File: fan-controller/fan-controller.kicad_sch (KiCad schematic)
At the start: 0 parts

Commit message: Add Seeed XIAO ESP32-C3 module to schematic
Vendored Seeed's official OPL KiCad library (symbol + SMD/DIP footprints)
for the XIAO series into fan-controller/libraries/, with project-local
sym-lib-table/fp-lib-table pointing at it. Placed U1 as the XIAO
ESP32-C3, using the DIP footprint (14 through-hole-style pads matching
the module's usable pins) since it'll be socketed via female headers
rather than soldered direct.
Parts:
- added U1: XIAO ESP32-C3, Seeed_Studio_XIAO_Series:XIAO-ESP32-C3-DIP, symbol Seeed_Studio_XIAO_Series:XIAO-ESP32-C3-SMD
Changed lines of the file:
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@@
 		)
 	)
+  (symbol (lib_id "Seeed_Studio_XIAO_Series:XIAO-ESP32-C3-SMD") (at 150.0 100.0 0) (unit 1)
+  (exclude_from_sim no) (in_bom yes) (on_board yes) (dnp no)
+  (property "Reference" "U1" (at 150.0 95.0 0)
+    (effects (font (size 1.27 1.27)))
+  )
+  (property "Value" "XIAO ESP32-C3" (at 150.0 102.54 0)
+    (effects (font (size 1.27 1.27)))
+  )
+  (property "Footprint" "Seeed_Studio_XIAO_Series:XIAO-ESP32-C3-DIP" (at 150.0 105.08 0)
+    (effects (font (size 1.27 1.27)) (hide yes))
+  )
+    (pin "1")
+    (pin "2")
+    (pin "3")
+    (pin "4")
+    (pin "5")
+    (pin "6")
+    (pin "7")
+    (pin "8")
+    (pin "9")
+    (pin "10")
+    (pin "11")
+    (pin "12")
+    (pin "13")
+    (pin "14")
+    (pin "15")
+    (pin "16")
+    (pin "17")
+    (pin "18")
+    (pin "19")
+    (pin "20")
+    (pin "21")
+    (pin "22")
 )
+)

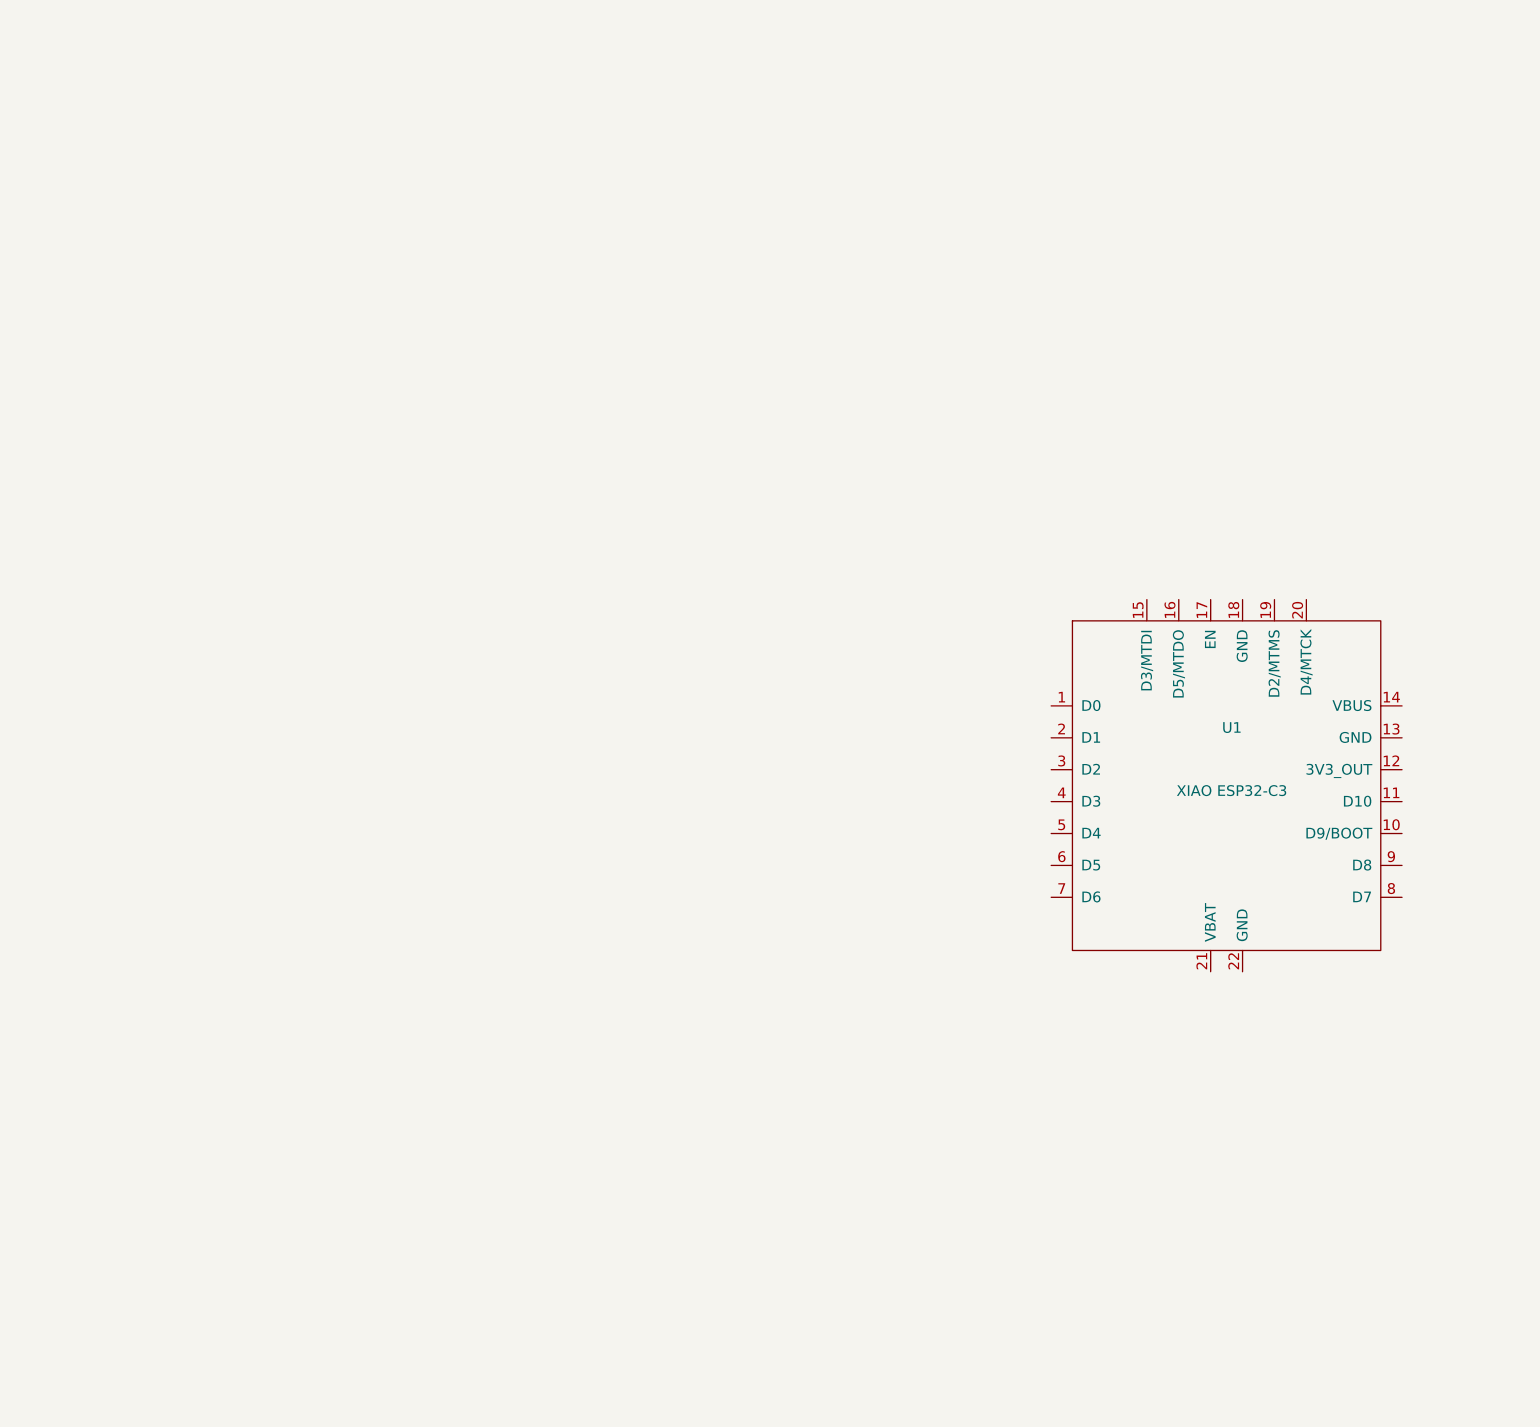
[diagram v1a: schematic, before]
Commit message: Place all remaining components and fix MCP-generated schematic corruption
Placed: 4x fan headers (J2-J5), 4x 10k tach pull-ups (R1-R4), 4x 1k PWM
series resistors (R5-R8), 4x 330R tach series resistors (R9-R12),
barrel jack reverse-polarity protection chain (J1/D1/F1/C1), and the
12V->5V regulator (U2, AMS1117-5.0 via base symbol AP1117-15) with
input/output caps.

Also fixed real defects in every component the kicad-mcp-server tool
placed, discovered by bisecting against kicad-cli (which the tool's own
"success" messages never actually validate against):
- add_component_from_library embeds an invalid (uuid ...) sub-field
  inside each property block on placed instances -- not valid KiCad 10
  schematic syntax, made the whole file fail to load ("Konnte
  Schaltplan nicht laden" / exit 3), despite the tool reporting success
- placed instances were missing the required (instances (project ...))
  block that associates them with this project/sheet
- sheet_instances must be the last top-level element, not positioned
  right after lib_symbols

Confirmed fixed via kicad-cli sch erc (loads cleanly, only expected
"pin not connected" warnings remain since nothing is wired yet).
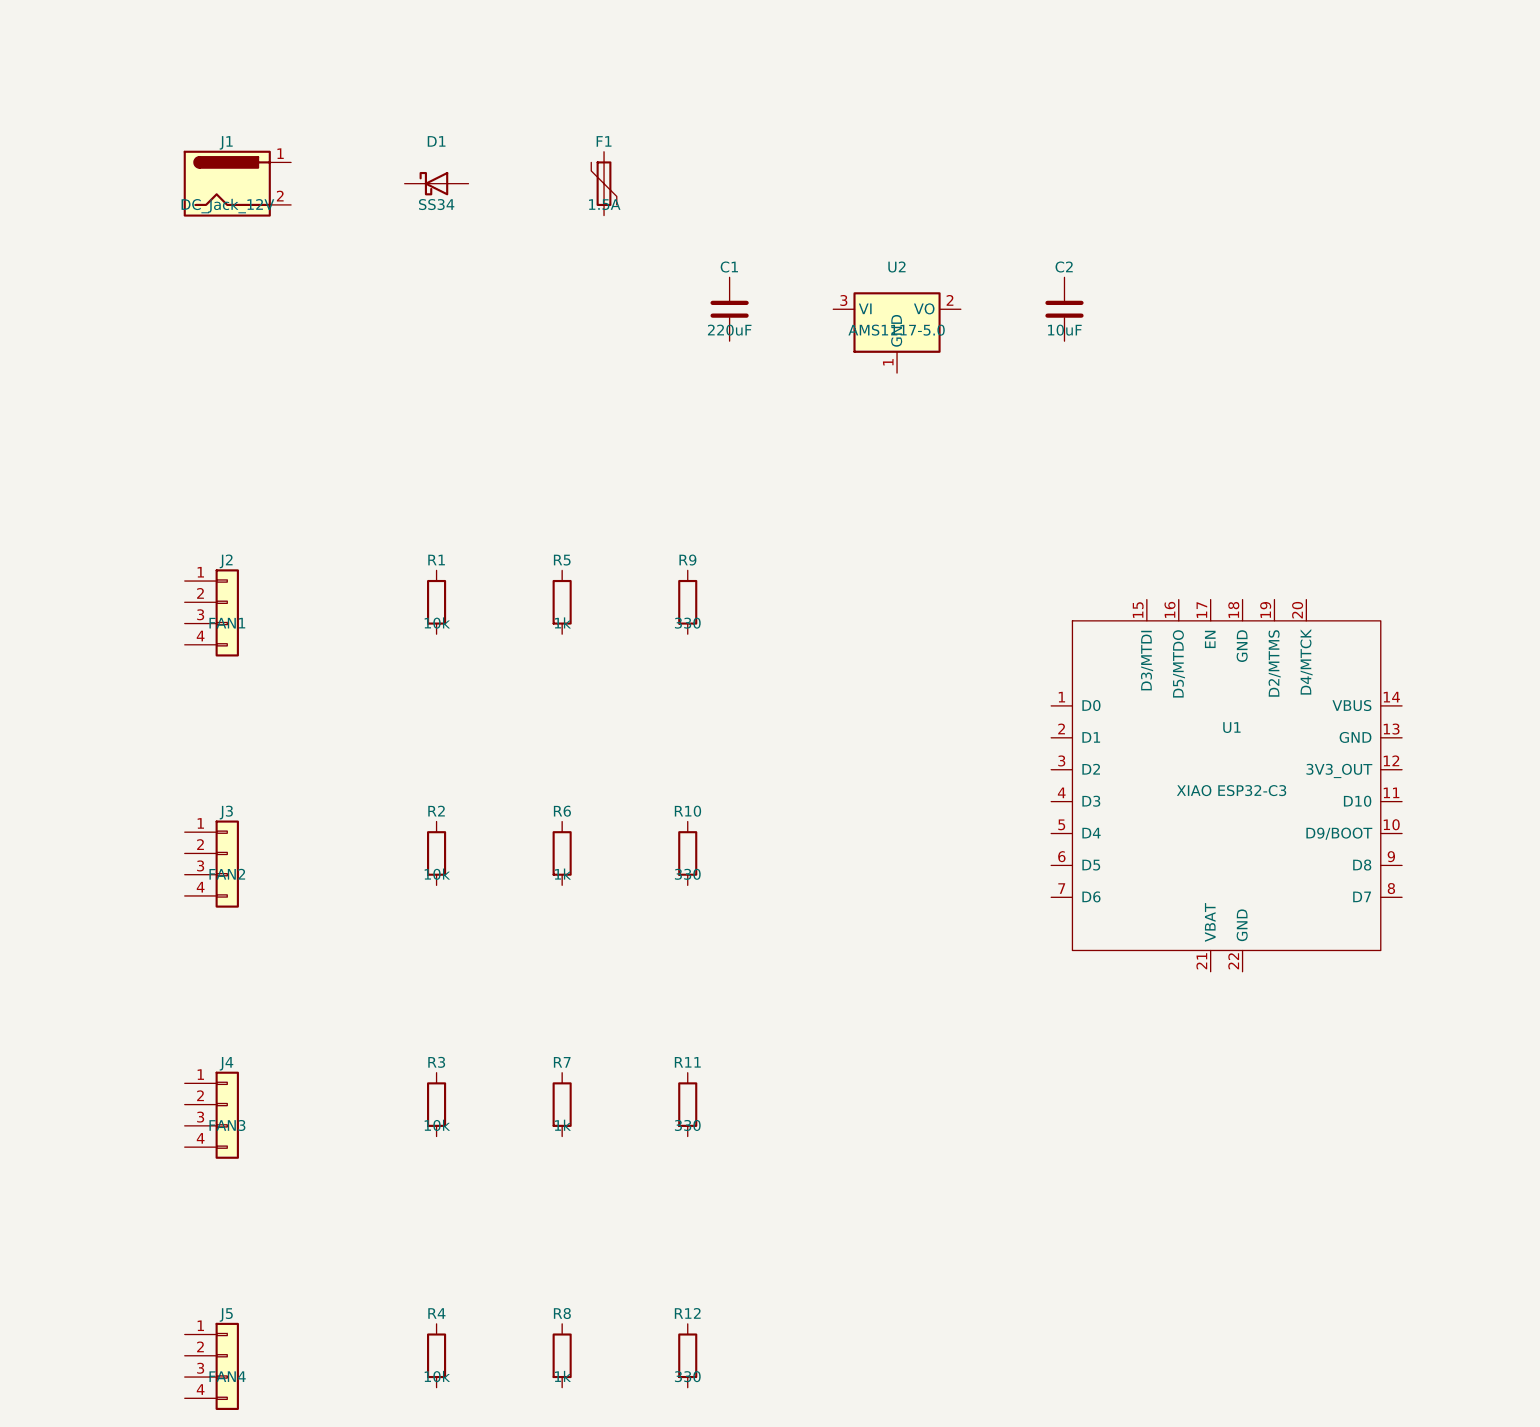
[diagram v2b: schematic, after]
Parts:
- added C1: 220uF, Capacitor_THT:CP_Radial_D8.0mm_P3.50mm, symbol Device:C
- added C2: 10uF, Capacitor_SMD:C_0805_2012Metric, symbol Device:C
- added D1: SS34, Diode_SMD:D_SMA, symbol Device:D_Schottky
- added F1: 1.5A, Fuse:Fuse_1812_4532Metric, symbol Device:Polyfuse
- added J1: DC_Jack_12V, Connector_BarrelJack:BarrelJack_CUI_PJ-102AH_Horizontal, symbol Connector:Barrel_Jack
- added J2: FAN1, Connector_PinHeader_2.54mm:PinHeader_1x04_P2.54mm_Vertical, symbol Connector_Generic:Conn_01x04
- added J3: FAN2, Connector_PinHeader_2.54mm:PinHeader_1x04_P2.54mm_Vertical, symbol Connector_Generic:Conn_01x04
- added J4: FAN3, Connector_PinHeader_2.54mm:PinHeader_1x04_P2.54mm_Vertical, symbol Connector_Generic:Conn_01x04
- added J5: FAN4, Connector_PinHeader_2.54mm:PinHeader_1x04_P2.54mm_Vertical, symbol Connector_Generic:Conn_01x04
- added R1, R2, R3, R4: 10k, Resistor_SMD:R_0603_1608Metric, symbol Device:R
- added R10, R11, R12, R9: 330, Resistor_SMD:R_0603_1608Metric, symbol Device:R
- added R5, R6, R7, R8: 1k, Resistor_SMD:R_0603_1608Metric, symbol Device:R
- added U2: AMS1117-5.0, Package_TO_SOT_SMD:SOT-223-3_TabPin2, symbol Regulator_Linear:AP1117-15

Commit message: Wire the complete fan controller schematic
All 22 nets connected and verified pin-by-pin against the netlist:

  Power:  J1 -> D1 (reverse-polarity) -> F1 (polyfuse) -> +12V_PROT
          +12V_PROT -> C1, U2 (AMS1117-5.0) -> +5V -> C2, XIAO VBUS
          XIAO 3V3_OUT -> four 10k tach pull-ups
  Fans:   each J: pin1 GND, pin2 +12V_PROT, pin3 tach, pin4 PWM
          tach -> 10k pull-up to 3V3, then 330R series -> XIAO
          XIAO -> 1k series -> fan PWM
  GPIO:   FAN1 D1/D2  FAN2 D3/D4  FAN3 D5/D6  FAN4 D7/D10
          D0, D8, D9 left free (ESP32-C3 strapping pins)

Wired as per-pin stubs plus net labels rather than routed traces, so
there are no shared routing lanes and therefore no collinear T-tap
shorts. Geometry generated from a pin table extracted programmatically
from the file, not hand-typed.

The bug that broke both earlier attempts: symbol libraries use math
convention (+y up) while the schematic canvas uses screen convention
(+y down), so a pin's absolute position is place_y MINUS local_y, not
plus. Adding it mirrors every pin about its symbol origin, silently
attaching wires to the pin on the opposite side of the part (XIAO VBUS
resolved to D9/BOOT). ERC passes regardless, since landing on the wrong
real pin is still a valid connection - only a netlist audit catches it.

ERC: no electrical errors. Remaining 93 endpoint_off_grid warnings are
cosmetic, from the XIAO footprint's fractional pin pitch. PWR_FLAGs on
+12V_PROT and GND satisfy the power-pin-driven check; no_connect markers
mark the 9 deliberately unused XIAO pins.
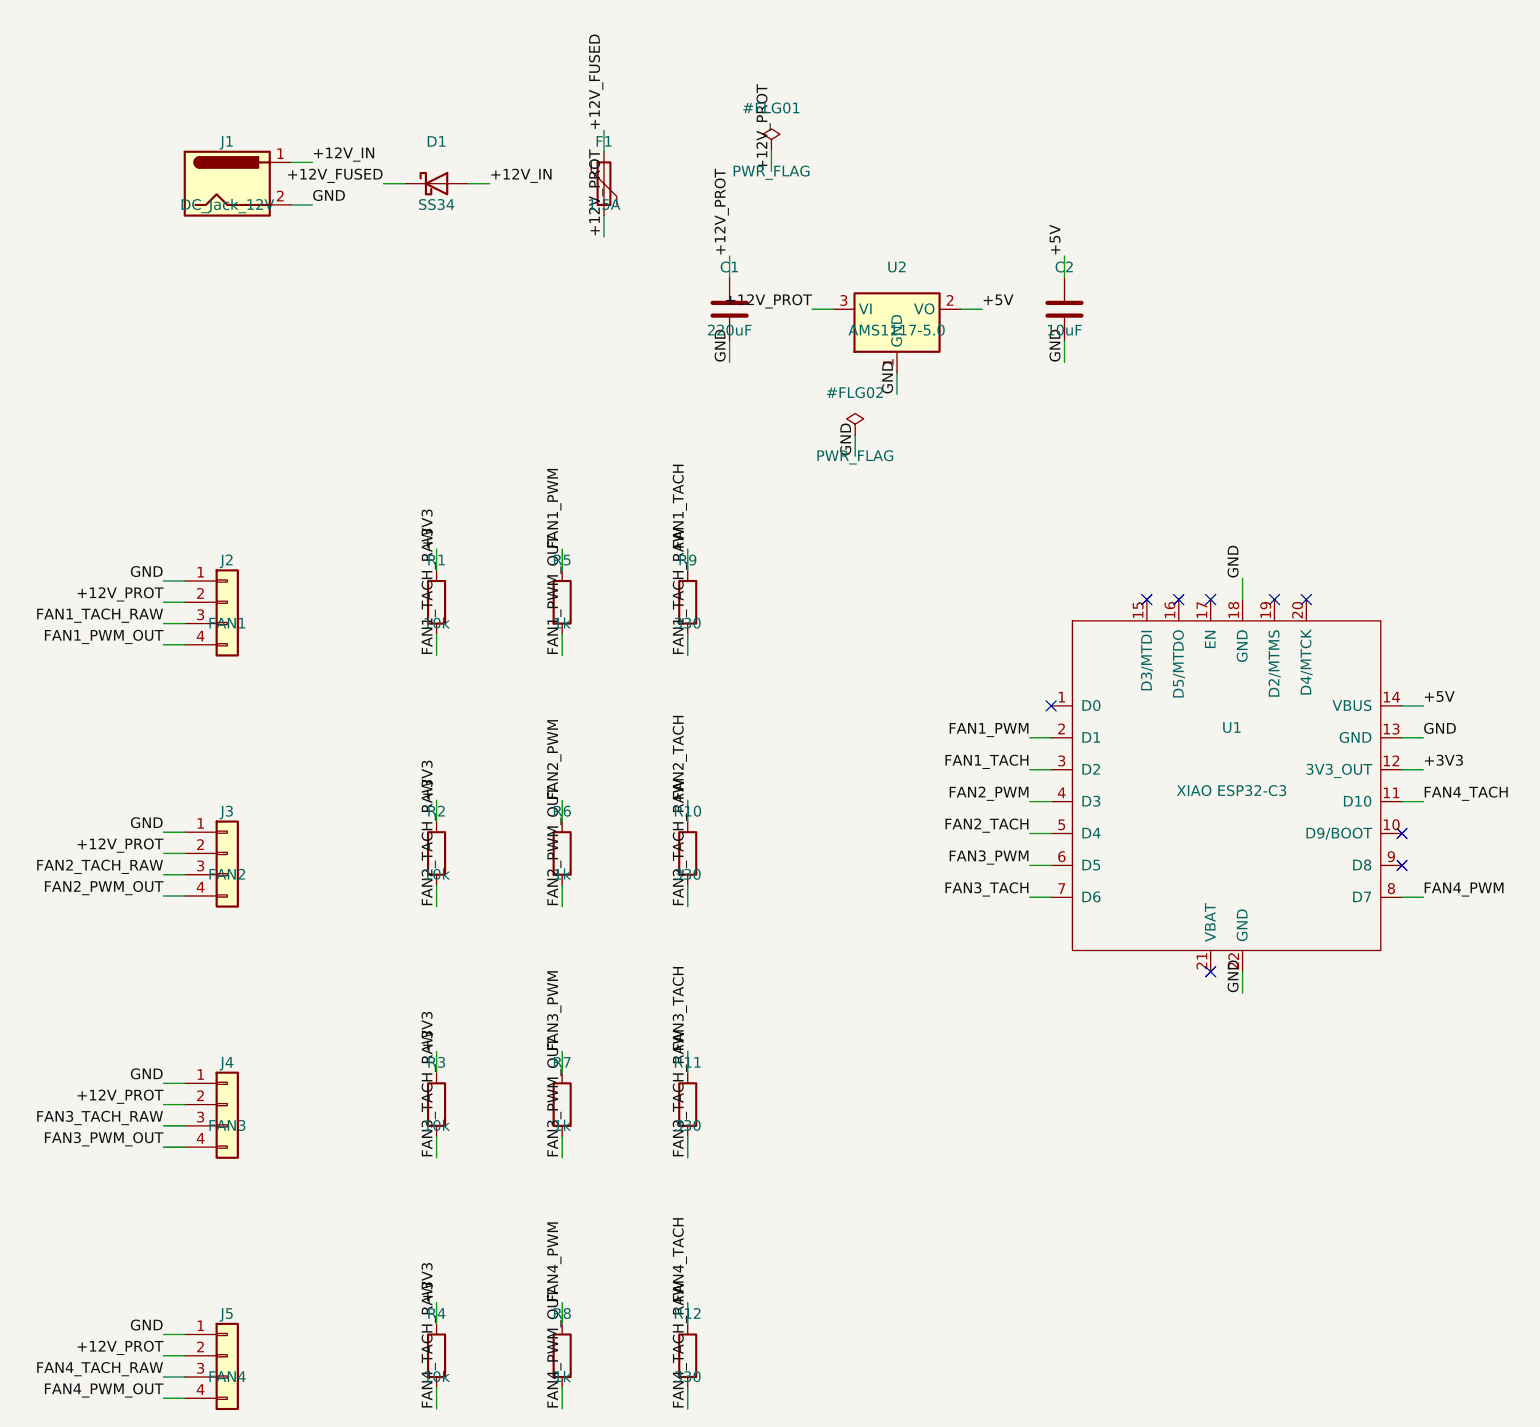
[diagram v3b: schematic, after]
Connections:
- net FAN3_PWM: now reaches R7.1
- net FAN3_PWM: now also U1.6 (D5)
- net FAN3_PWM_OUT: now reaches R7.2
- net FAN3_PWM_OUT: now also J4.4 (Pin_4)
- net FAN4_TACH: now reaches R12.1
- net FAN4_TACH: now also U1.11 (D10)
- net FAN4_TACH_RAW: now reaches R12.2
- net FAN4_TACH_RAW: now also J5.3 (Pin_3), R4.2
- net FAN3_TACH: now reaches R11.1
- net FAN3_TACH: now also U1.7 (D6)
- net FAN3_TACH_RAW: now reaches R11.2
- net FAN3_TACH_RAW: now also J4.3 (Pin_3), R3.2
- net FAN1_PWM: now reaches R5.1
- net FAN1_PWM: now also U1.2 (D1)
- net FAN1_PWM_OUT: now reaches R5.2
- net FAN1_PWM_OUT: now also J2.4 (Pin_4)
- net +12V_PROT: now reaches C1.1
- net +12V_PROT: now also F1.2, J2.2 (Pin_2), J3.2 (Pin_2), J4.2 (Pin_2), J5.2 (Pin_2), U2.3 (VI)
- net GND: now reaches C1.2
- net GND: now also C2.2, J1.2, J2.1 (Pin_1), J3.1 (Pin_1), J4.1 (Pin_1), J5.1 (Pin_1), U1.13 (GND), U1.18 (GND), U1.22 (GND), U2.1 (GND)
- net +3V3: now reaches R4.1
- net +3V3: now also R1.1, R2.1, R3.1, U1.12 (3V3_OUT)
- net FAN2_TACH_RAW: now reaches R2.2
- net FAN2_TACH_RAW: now also J3.3 (Pin_3), R10.2
- net FAN4_PWM: now reaches R8.1
- net FAN4_PWM: now also U1.8 (D7)
- net FAN4_PWM_OUT: now reaches R8.2
- net FAN4_PWM_OUT: now also J5.4 (Pin_4)
- net FAN1_TACH_RAW: now reaches J2.3 (Pin_3)
- net FAN1_TACH_RAW: now also R1.2, R9.2
- net FAN2_TACH: now reaches R10.1
- net FAN2_TACH: now also U1.5 (D4)
- net FAN1_TACH: now reaches R9.1
- net FAN1_TACH: now also U1.3 (D2)
- net +12V_FUSED: now reaches F1.1
- net +12V_FUSED: now also D1.1 (K)
- net +5V: now reaches U2.2 (VO)
- net +5V: now also C2.1, U1.14 (VBUS)
- net +12V_IN: now reaches J1.1
- net +12V_IN: now also D1.2 (A)
- net FAN2_PWM: now reaches U1.4 (D3)
- net FAN2_PWM: now also R6.1
- net FAN2_PWM_OUT: now reaches J3.4 (Pin_4)
- net FAN2_PWM_OUT: now also R6.2
- no-connect marks 0 -> 9
